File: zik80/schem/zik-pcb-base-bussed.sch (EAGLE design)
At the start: 55 parts, among them IC1 7432N, IC2 7404N

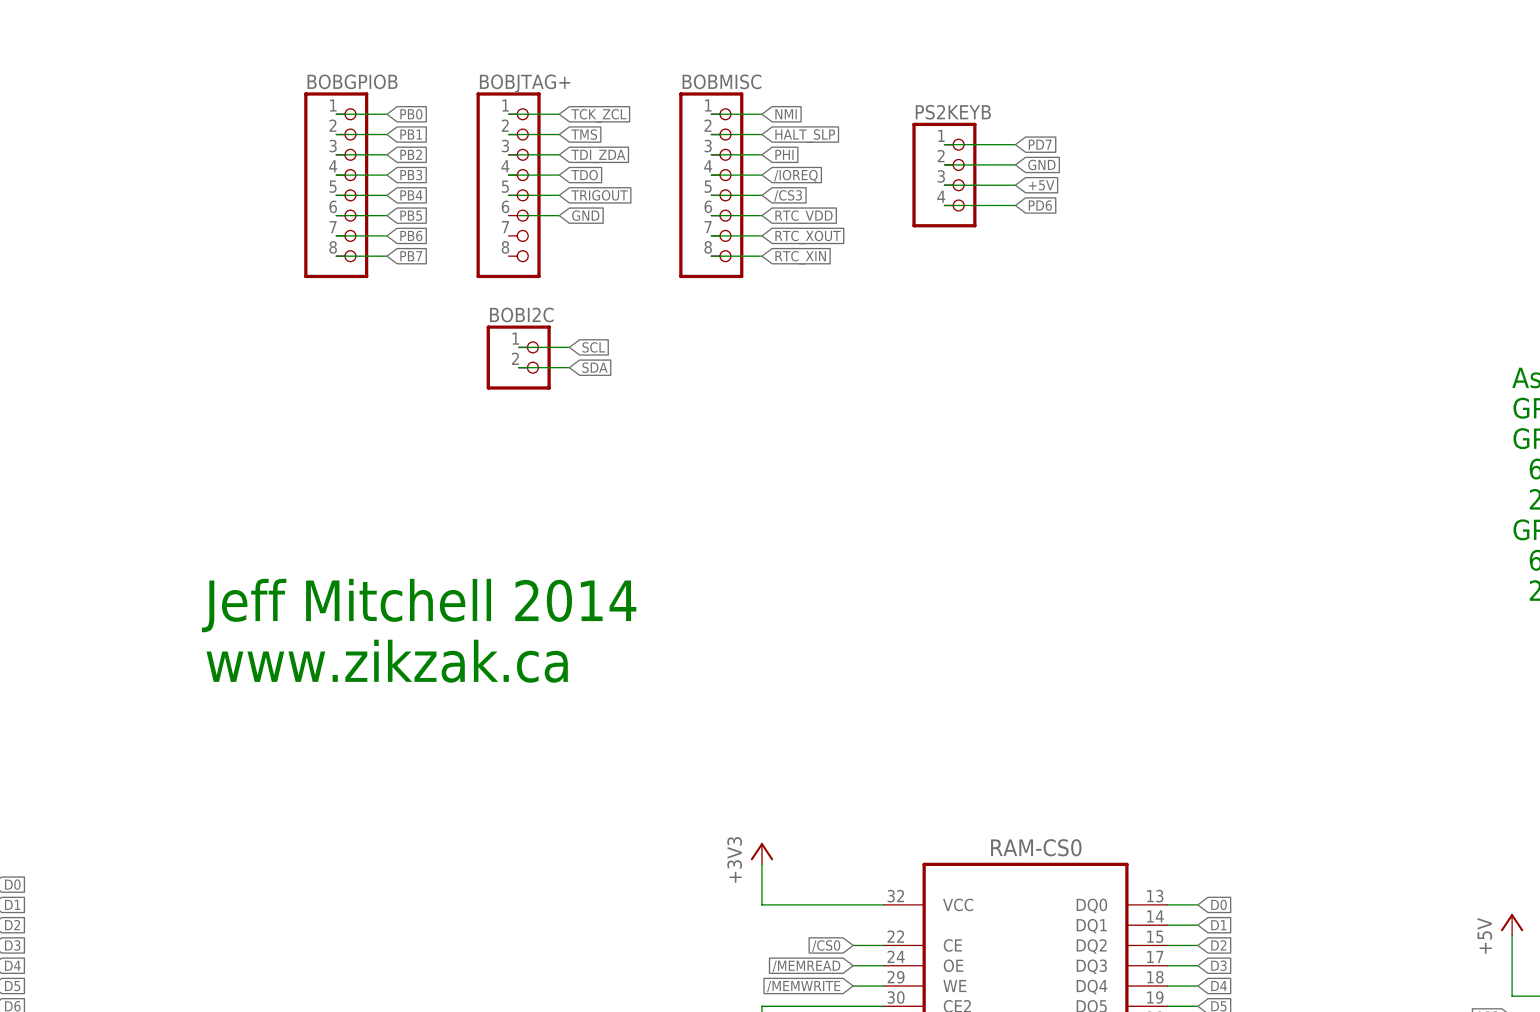
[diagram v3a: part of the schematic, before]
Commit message: Working on base pcb .. only about 20 more traces to go/cheat. Whew. Terrible mess, but maybe it'll work.. really needs larger pcb or more planes :O
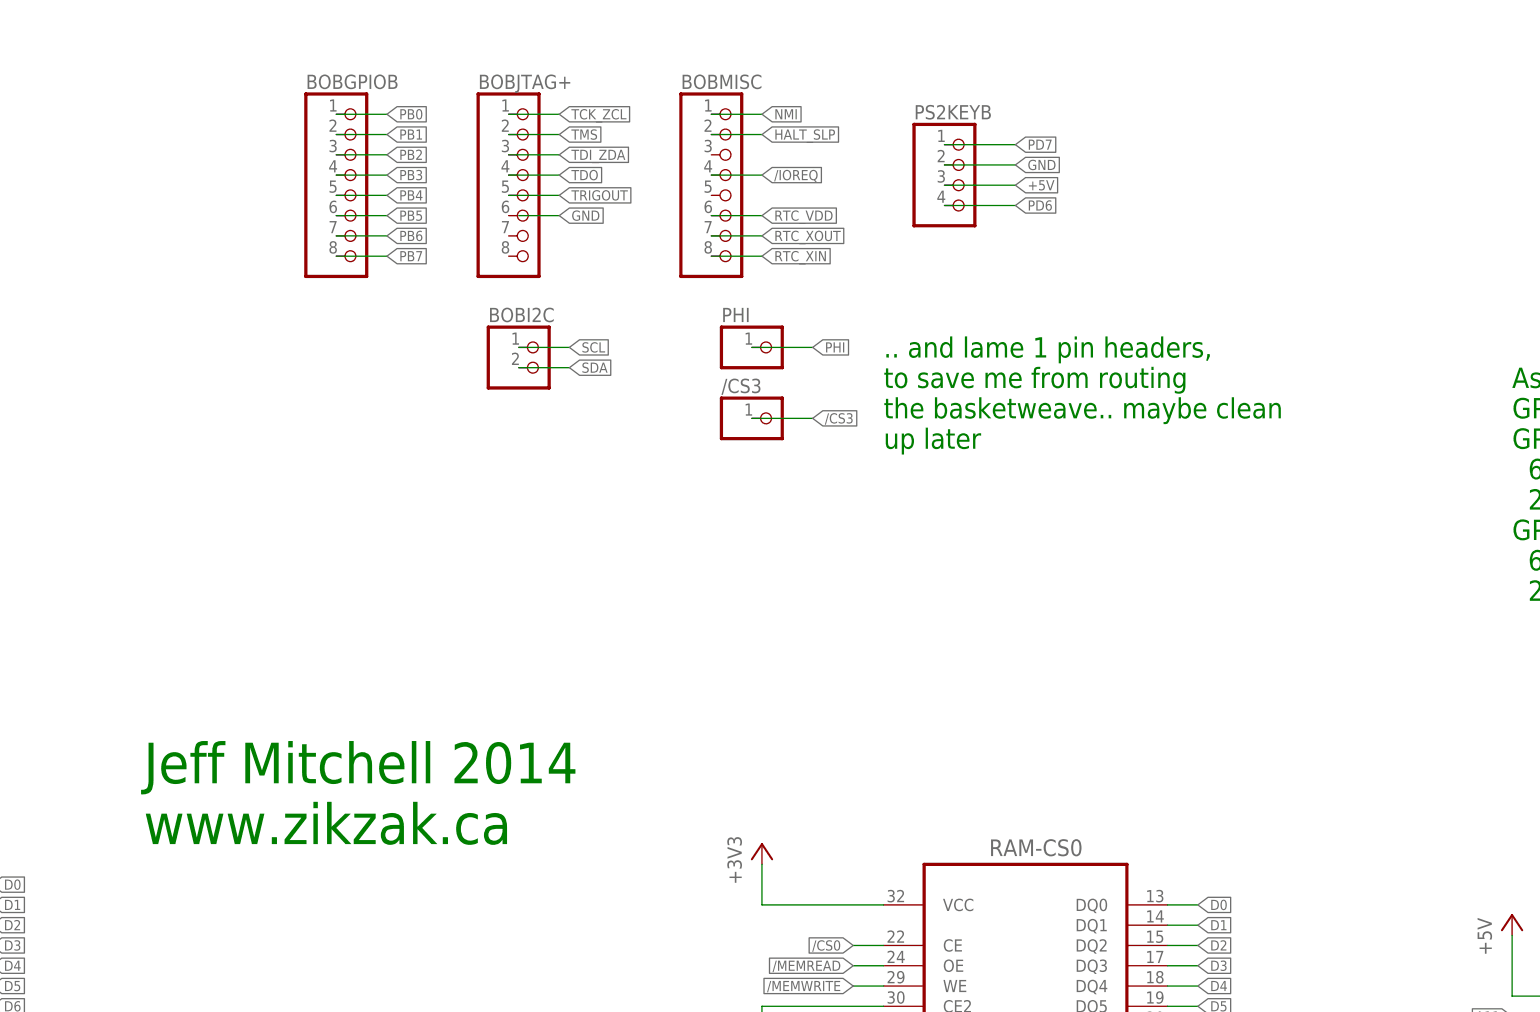
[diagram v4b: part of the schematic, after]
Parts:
- added /CS3, PHI: (no value), pinhead:PINHD-1X1
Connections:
- net /CS3: now also /CS3.1; no longer BOBMISC.5
- net PHI: now also PHI.1; no longer BOBMISC.3
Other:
- note added: ".. and lame 1 pin headers, to save me from routing the basketweave.. maybe clean up later"
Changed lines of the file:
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@@
 <part name="GND22" library="supply1" deviceset="GND" device=""/>
 <part name="BOBI2C" library="pinhead" deviceset="PINHD-1X2" device=""/>
+<part name="PHI" library="pinhead" deviceset="PINHD-1X1" device=""/>
+<part name="/CS3" library="pinhead" deviceset="PINHD-1X1" device=""/>
 </parts>
 <sheets>
@@
   6 for joy-2
   2 for keyb</text>
-<text x="140.97" y="191.77" size="5.08" layer="91">Jeff Mitchell 2014
+<text x="133.35" y="171.45" size="5.08" layer="91">Jeff Mitchell 2014
 www.zikzak.ca</text>
+<text x="226.06" y="220.98" size="2.54" layer="91">.. and lame 1 pin headers,
+to save me from routing
+the basketweave.. maybe clean
+up later</text>
 </plain>
 <instances>
@@
 <instance part="GND22" gate="1" x="401.32" y="256.54" rot="R270"/>
 <instance part="BOBI2C" gate="G$1" x="182.88" y="231.14"/>
+<instance part="PHI" gate="G$1" x="212.09" y="233.68"/>
+<instance part="/CS3" gate="G$1" x="212.09" y="224.79"/>
 </instances>
 <busses>
@@
 </segment>
 <segment>
-<pinref part="BOBMISC" gate="A" pin="3"/>
-<wire x1="204.47" y1="257.81" x2="210.82" y2="257.81" width="0.1524" layer="91"/>
-<label x="210.82" y="257.81" size="1.27" layer="95" xref="yes"/>
+<pinref part="PHI" gate="G$1" pin="1"/>
+<wire x1="209.55" y1="233.68" x2="217.17" y2="233.68" width="0.1524" layer="91"/>
+<label x="217.17" y="233.68" size="1.27" layer="95" xref="yes"/>
 </segment>
 </net>
@@
 </segment>
 <segment>
-<wire x1="204.47" y1="252.73" x2="210.82" y2="252.73" width="0.1524" layer="91"/>
-<label x="210.82" y="252.73" size="1.27" layer="95" xref="yes"/>
-<pinref part="BOBMISC" gate="A" pin="5"/>
-</segment>
-</net>
+<pinref part="/CS3" gate="G$1" pin="1"/>
+<wire x1="209.55" y1="224.79" x2="217.17" y2="224.79" width="0.1524" layer="91"/>
+<label x="217.17" y="224.79" size="1.27" layer="95" xref="yes"/>
+</segment>
+</net>

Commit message: zikzak base pcb rev1 sent to boardhouse :)
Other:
- note added: "- Big Question: V-in-low and V-in-high from eZ80 to 74HC32-at-3.3 are close --> could bodge 5v into 73LS32 and it should work - GPIO PB unused -> sent to BoB for LEDs/switches - rev2: IOREQ, handle OUT for something/BoB? - rev2: amplifier 2n2222 as per http below? mix all 3 channels together to another pin on speaker header? amp on board? - rev2: ?? put PSG back onto GPIO PB, drop the inverters, 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"
- note removed: "- brd positions - drill holes - identification stamp - Big Question: V-in-low and V-in-high from eZ80 to 74HC32-at-3.3 are close --> could bodge 5v into 73LS32 and it should work - GPIO PB unused -> sent to BoB for LEDs/switches - rev2: IOREQ, handle OUT for something/BoB? - rev2: amplifier 2n2222 as per http below? mix all 3 channels together to another pin on speaker header? amp on board? - rev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"
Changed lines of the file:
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@@
 <setting verticaltext="up"/>
 </settings>
-<grid distance="0.05" unitdist="inch" unit="inch" style="dots" multiple="1" display="yes" altdistance="0.01" altunitdist="inch" altunit="inch"/>
+<grid distance="0.05" unitdist="inch" unit="inch" style="lines" multiple="1" display="no" altdistance="0.01" altunitdist="inch" altunit="inch"/>
 <layers>
 <layer number="1" name="Top" color="4" fill="1" visible="no" active="no"/>
@@
 <plain>
 <rectangle x1="21.59" y1="-207.518" x2="100.584" y2="-190.5" layer="206"/>
-<text x="213.36" y="-62.23" size="5.08" layer="91">- brd positions
-- drill holes
-- identification stamp
-- Big Question: V-in-low and V-in-high from eZ80 to 74HC32-at-3.3 are close
+<text x="214.63" y="-30.48" size="5.08" layer="91">- Big Question: V-in-low and V-in-high from eZ80 to 74HC32-at-3.3 are close
 --&gt; could bodge 5v into 73LS32 and it should work
 - GPIO PB unused -&gt; sent to BoB for LEDs/switches
@@
 <net name="/BUSREQ" class="0">
 <segment>
-<wire x1="425.45" y1="107.95" x2="416.56" y2="107.95" width="0.1524" layer="91"/>
 <pinref part="CTRL_BUS" gate="A" pin="13"/>
-<label x="416.56" y="107.95" size="1.27" layer="95" rot="R180" xref="yes"/>
 <pinref part="CTRL_BUS" gate="A" pin="14"/>
 <wire x1="425.45" y1="107.95" x2="433.07" y2="107.95" width="0.1524" layer="91"/>
+<wire x1="425.45" y1="107.95" x2="416.56" y2="107.95" width="0.1524" layer="91"/>
+<label x="416.56" y="107.95" size="1.27" layer="95" rot="R180" xref="yes"/>
 <junction x="425.45" y="107.95"/>
 </segment>
@@
 <net name="/BUSACK" class="0">
 <segment>
-<wire x1="425.45" y1="105.41" x2="416.56" y2="105.41" width="0.1524" layer="91"/>
 <pinref part="CTRL_BUS" gate="A" pin="15"/>
-<label x="416.56" y="105.41" size="1.27" layer="95" rot="R180" xref="yes"/>
 <pinref part="CTRL_BUS" gate="A" pin="16"/>
 <wire x1="425.45" y1="105.41" x2="433.07" y2="105.41" width="0.1524" layer="91"/>
+<wire x1="425.45" y1="105.41" x2="416.56" y2="105.41" width="0.1524" layer="91"/>
+<label x="416.56" y="105.41" size="1.27" layer="95" rot="R180" xref="yes"/>
 <junction x="425.45" y="105.41"/>
 </segment>

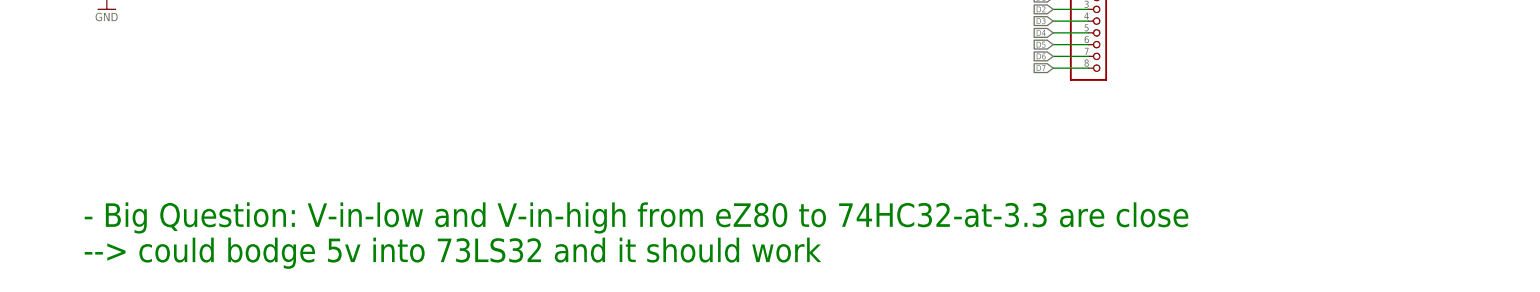
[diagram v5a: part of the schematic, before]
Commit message: Fiddling with hooking up the gpu and cpu buses .. need more IDC connector!
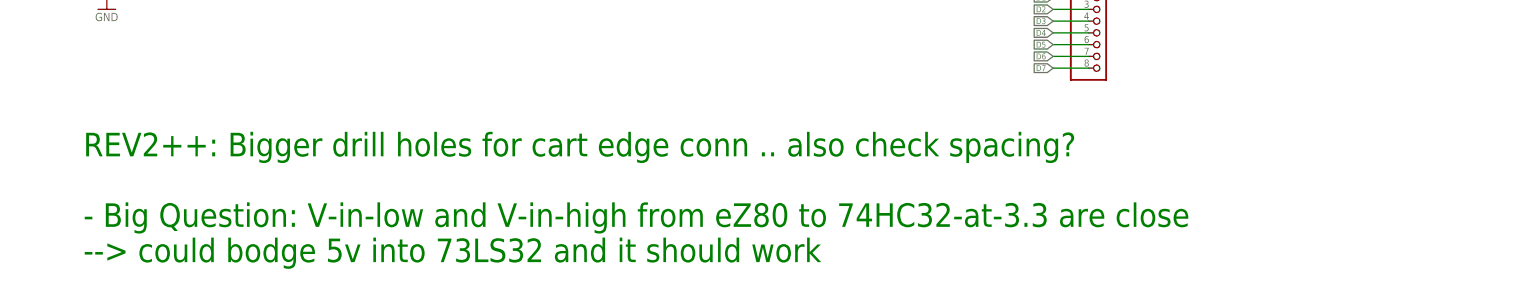
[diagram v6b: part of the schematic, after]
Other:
- note added: "REV2++: Bigger drill holes for cart edge conn .. also check spacing? - Big Question: V-in-low and V-in-high from eZ80 to 74HC32-at-3.3 are close --> could bodge 5v into 73LS32 and it should work - GPIO PB unused -> sent to BoB for LEDs/switches - rev2: IOREQ, handle OUT for something/BoB? - rev2: amplifier 2n2222 as per http below? mix all 3 channels together to another pin on speaker header? amp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"
- note removed: "- Big Question: V-in-low and V-in-high from eZ80 to 74HC32-at-3.3 are close --> could bodge 5v into 73LS32 and it should work - GPIO PB unused -> sent to BoB for LEDs/switches - rev2: IOREQ, handle OUT for something/BoB? - rev2: amplifier 2n2222 as per http below? mix all 3 channels together to another pin on speaker header? amp on board? - rev2: ?? put PSG back onto GPIO PB, drop the inverters, 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"
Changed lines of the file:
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@@
 <setting verticaltext="up"/>
 </settings>
-<grid distance="0.05" unitdist="inch" unit="inch" style="lines" multiple="1" display="no" altdistance="0.01" altunitdist="inch" altunit="inch"/>
+<grid distance="0.1" unitdist="inch" unit="inch" style="lines" multiple="1" display="no" altdistance="0.01" altunitdist="inch" altunit="inch"/>
 <layers>
 <layer number="1" name="Top" color="4" fill="1" visible="no" active="no"/>
@@
 <plain>
 <rectangle x1="21.59" y1="-207.518" x2="100.584" y2="-190.5" layer="206"/>
-<text x="214.63" y="-30.48" size="5.08" layer="91">- Big Question: V-in-low and V-in-high from eZ80 to 74HC32-at-3.3 are close
+<text x="214.63" y="-30.48" size="5.08" layer="91">REV2++: Bigger drill holes for cart edge conn .. also check spacing?
+- Big Question: V-in-low and V-in-high from eZ80 to 74HC32-at-3.3 are close
 --&gt; could bodge 5v into 73LS32 and it should work
 - GPIO PB unused -&gt; sent to BoB for LEDs/switches

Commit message: Full success! eZ80 -> RAM -> GPU
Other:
- note added: "REV2++: Bigger drill holes for cart edge conn .. also check spacing? ++ split off addr to 16+6 connectors ++ CHG edge connector to side mount with pads, instead of drill holes at all; just squish the pins or pads and solder! ++ Clear space around audio osc .. esp resistor needs to move - Big Question: V-in-low and V-in-high from eZ80 to 74HC32-at-3.3 are close --> could bodge 5v into 73LS32 and i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"
- note removed: "REV2++: Bigger drill holes for cart edge conn .. also check spacing? - Big Question: V-in-low and V-in-high from eZ80 to 74HC32-at-3.3 are close --> could bodge 5v into 73LS32 and it should work - GPIO PB unused -> sent to BoB for LEDs/switches - rev2: IOREQ, handle OUT for something/BoB? - rev2: amplifier 2n2222 as per http below? mix all 3 channels together to another pin on speaker header? amp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"
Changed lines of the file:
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@@
 <plain>
 <rectangle x1="21.59" y1="-207.518" x2="100.584" y2="-190.5" layer="206"/>
-<text x="214.63" y="-30.48" size="5.08" layer="91">REV2++: Bigger drill holes for cart edge conn .. also check spacing?
+<text x="214.63" y="-45.72" size="5.08" layer="91">REV2++: Bigger drill holes for cart edge conn .. also check spacing?
+++ split off addr to 16+6 connectors
+++ CHG edge connector to side mount with pads, instead of drill holes at all; just squish the pins or pads and solder!
+++ Clear space around audio osc .. esp resistor needs to move
 - Big Question: V-in-low and V-in-high from eZ80 to 74HC32-at-3.3 are close
 --&gt; could bodge 5v into 73LS32 and it should work

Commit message: SBC pcb design rev2, sprite demo on ARM
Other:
- note added: "!! Needs pull-ups on ps/2 keyb! REV2++: Bigger drill holes for cart edge conn .. also check spacing? ++ split off addr to 16+6 connectors ++ CHG edge connector to side mount with pads, instead of drill holes at all; just squish the pins or pads and solder! ++ Clear space around audio osc .. esp resistor needs to move - Big Question: V-in-low and V-in-high from eZ80 to 74HC32-at-3.3 are close --> 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"
- note removed: "REV2++: Bigger drill holes for cart edge conn .. also check spacing? ++ split off addr to 16+6 connectors ++ CHG edge connector to side mount with pads, instead of drill holes at all; just squish the pins or pads and solder! ++ Clear space around audio osc .. esp resistor needs to move - Big Question: V-in-low and V-in-high from eZ80 to 74HC32-at-3.3 are close --> could bodge 5v into 73LS32 and i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"
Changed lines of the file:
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@@
 <plain>
 <rectangle x1="21.59" y1="-207.518" x2="100.584" y2="-190.5" layer="206"/>
-<text x="214.63" y="-45.72" size="5.08" layer="91">REV2++: Bigger drill holes for cart edge conn .. also check spacing?
+<text x="222.25" y="-78.74" size="5.08" layer="91">!! Needs pull-ups on ps/2 keyb!
+REV2++: Bigger drill holes for cart edge conn .. also check spacing?
 ++ split off addr to 16+6 connectors
 ++ CHG edge connector to side mount with pads, instead of drill holes at all; just squish the pins or pads and solder!
